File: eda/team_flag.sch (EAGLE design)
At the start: 19 parts, among them Q1 IRFML8244, Q2 IRFML8244

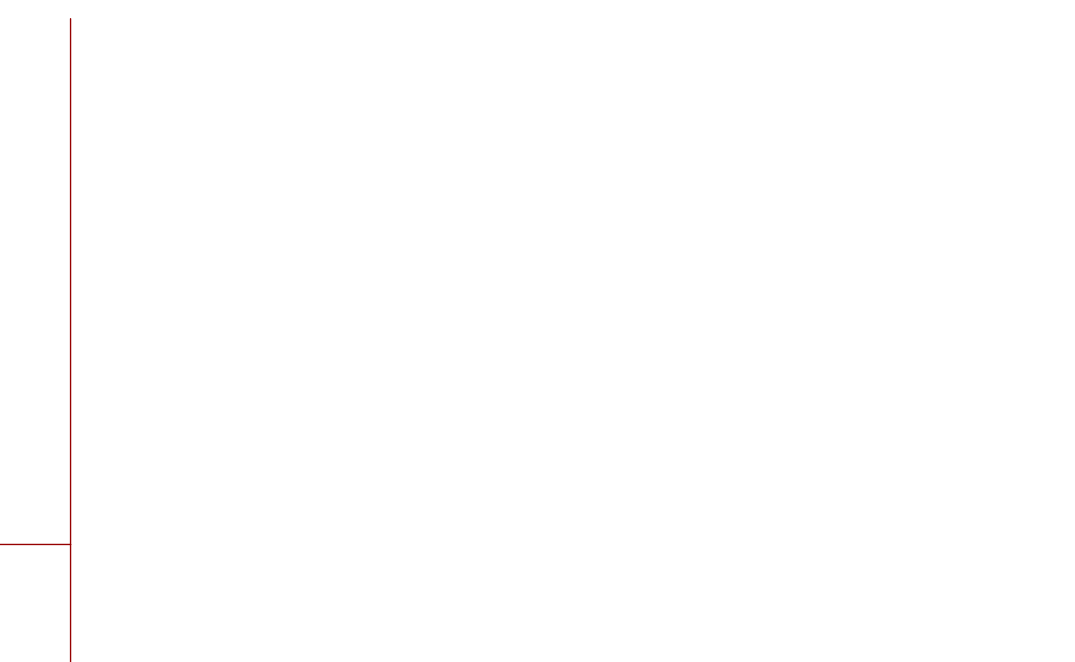
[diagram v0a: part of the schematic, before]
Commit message: Add Arduino Pro Micro breakout and connect nets on schematic
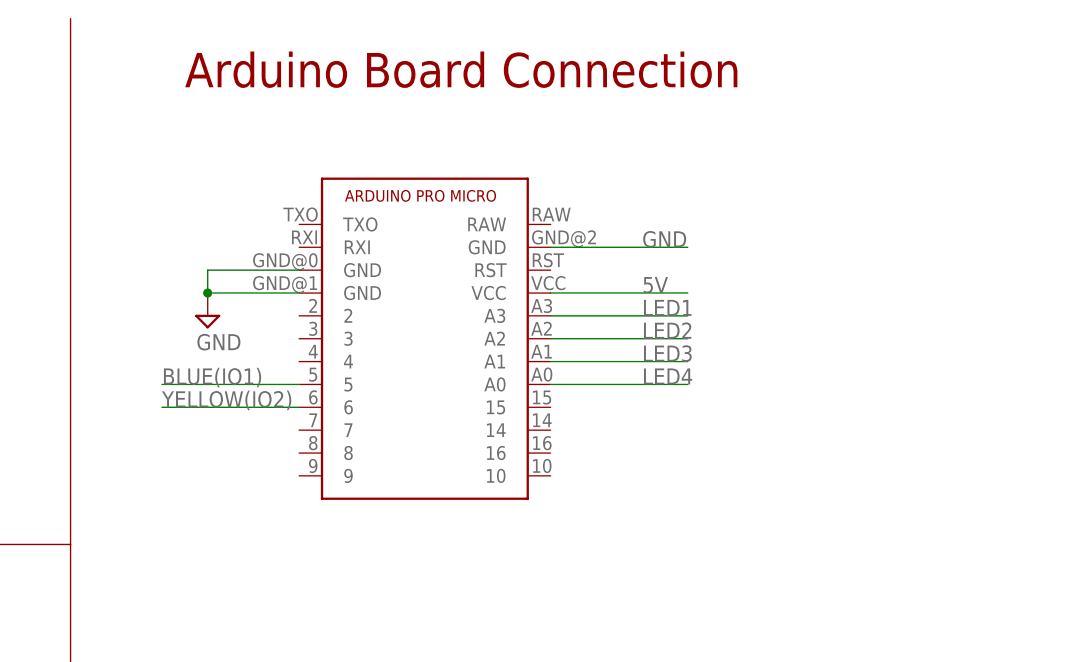
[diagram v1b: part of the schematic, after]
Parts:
- added U$3: ARDUINO_PRO_MICRO, pie:ARDUINO_PRO_MICRO
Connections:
- net 5V: now also U$3.VCC
- net BLUE(IO1): now also U$3.5
- net GND: now also U$3.GND@0, U$3.GND@1, U$3.GND@2
- net LED1: now also U$3.A3
- net LED2: now also U$3.A2
- net LED3: now also U$3.A1
- net LED4: now also U$3.A0
- net YELLOW(IO2): now also U$3.6
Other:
- note added: "Arduino Board Connection"
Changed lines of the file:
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@@
 <layer number="54" name="bGND_GNDA" color="1" fill="9" visible="no" active="no"/>
 <layer number="56" name="wert" color="7" fill="1" visible="no" active="no"/>
+<layer number="57" name="tCAD" color="7" fill="1" visible="no" active="no"/>
+<layer number="59" name="tCarbon" color="7" fill="1" visible="no" active="no"/>
+<layer number="60" name="bCarbon" color="7" fill="1" visible="no" active="no"/>
 <layer number="90" name="Modules" color="5" fill="1" visible="yes" active="yes"/>
 <layer number="91" name="Nets" color="2" fill="1" visible="yes" active="yes"/>
@@
 <layer number="109" name="fp9" color="7" fill="1" visible="yes" active="yes"/>
 <layer number="110" name="fp0" color="7" fill="1" visible="yes" active="yes"/>
+<layer number="111" name="LPC17xx" color="7" fill="1" visible="yes" active="yes"/>
+<layer number="112" name="tSilk" color="7" fill="1" visible="yes" active="yes"/>
+<layer number="113" name="IDFDebug" color="7" fill="1" visible="yes" active="yes"/>
+<layer number="114" name="Badge_Outline" color="11" fill="1" visible="no" active="no"/>
 <layer number="116" name="Patch_BOT" color="9" fill="4" visible="yes" active="yes"/>
+<layer number="118" name="Rect_Pads" color="7" fill="1" visible="yes" active="yes"/>
 <layer number="121" name="_tsilk" color="7" fill="1" visible="yes" active="yes"/>
 <layer number="122" name="_bsilk" color="7" fill="1" visible="yes" active="yes"/>
@@
 <layer number="124" name="bTestmark" color="7" fill="1" visible="yes" active="yes"/>
 <layer number="125" name="_tNames" color="7" fill="1" visible="yes" active="yes"/>
+<layer number="126" name="_bNames" color="7" fill="1" visible="yes" active="yes"/>
+<layer number="127" name="_tValues" color="7" fill="1" visible="yes" active="yes"/>
+<layer number="128" name="_bValues" color="7" fill="1" visible="yes" active="yes"/>
+<layer number="129" name="Mask" color="7" fill="1" visible="yes" active="yes"/>
 <layer number="131" name="tAdjust" color="7" fill="1" visible="yes" active="yes"/>
 <layer number="132" name="bAdjust" color="7" fill="1" visible="yes" active="yes"/>
 <layer number="144" name="Drill_legend" color="7" fill="1" visible="yes" active="yes"/>
+<layer number="150" name="Notes" color="7" fill="1" visible="yes" active="yes"/>
 <layer number="151" name="HeatSink" color="7" fill="1" visible="yes" active="yes"/>
+<layer number="152" name="_bDocu" color="7" fill="1" visible="yes" active="yes"/>
+<layer number="153" name="FabDoc1" color="7" fill="1" visible="yes" active="yes"/>
+<layer number="154" name="FabDoc2" color="7" fill="1" visible="yes" active="yes"/>
+<layer number="155" name="FabDoc3" color="7" fill="1" visible="yes" active="yes"/>
 <layer number="199" name="Contour" color="7" fill="1" visible="yes" active="yes"/>
 <layer number="200" name="200bmp" color="1" fill="10" visible="yes" active="yes"/>
@@
 <layer number="223" name="223bmp" color="24" fill="1" visible="no" active="no"/>
 <layer number="224" name="224bmp" color="25" fill="1" visible="no" active="no"/>
+<layer number="225" name="225bmp" color="7" fill="1" visible="yes" active="yes"/>
+<layer number="226" name="226bmp" color="7" fill="1" visible="yes" active="yes"/>
+<layer number="227" name="227bmp" color="7" fill="1" visible="yes" active="yes"/>
+<layer number="228" name="228bmp" color="7" fill="1" visible="yes" active="yes"/>
+<layer number="229" name="229bmp" color="7" fill="1" visible="yes" active="yes"/>
+<layer number="230" name="230bmp" color="7" fill="1" visible="yes" active="yes"/>
+<layer number="231" name="231bmp" color="7" fill="1" visible="yes" active="yes"/>
+<layer number="248" name="Housing" color="7" fill="1" visible="yes" active="yes"/>
+<layer number="249" name="Edge" color="7" fill="1" visible="yes" active="yes"/>
 <layer number="250" name="Descript" color="3" fill="1" visible="no" active="no"/>
 <layer number="251" name="SMDround" color="12" fill="11" visible="no" active="no"/>
 <layer number="254" name="cooling" color="7" fill="1" visible="yes" active="yes"/>
+<layer number="255" name="routoute" color="7" fill="1" visible="yes" active="yes"/>
 </layers>
 <schematic xreflabel="%F%N/%S.%C%R" xrefpart="/%S.%C%R">
@@
 <part name="LED4" library="pie" deviceset="LED" device="0805" value="RED"/>
 <part name="SUPPLY5" library="pie" deviceset="GND" device=""/>
+<part name="U$3" library="pie" deviceset="ARDUINO_PRO_MICRO" device=""/>
+<part name="SUPPLY6" library="pie" deviceset="GND" device=""/>
 </parts>
 <sheets>
@@
 <wire x1="109.22" y1="86.36" x2="109.22" y2="27.94" width="0.1524" layer="94"/>
 <wire x1="109.22" y1="27.94" x2="0" y2="27.94" width="0.1524" layer="94"/>
+<text x="121.92" y="177.8" size="3.81" layer="94" font="vector">Arduino Board Connection</text>
 </plain>
 <instances>
@@
 </instance>
 <instance part="SUPPLY5" gate="GND" x="78.74" y="35.56"/>
+<instance part="U$3" gate="G$1" x="147.32" y="149.86"/>
+<instance part="SUPPLY6" gate="GND" x="124.46" y="152.4"/>
 </instances>
 <busses>
@@
 <pinref part="JP2" gate="A" pin="4"/>
 <wire x1="27.94" y1="101.6" x2="48.26" y2="101.6" width="0.1524" layer="91"/>
+</segment>
+<segment>
+<pinref part="U$3" gate="G$1" pin="6"/>
+<label x="119.38" y="142.24" size="1.778" layer="95"/>
+<wire x1="134.62" y1="142.24" x2="119.38" y2="142.24" width="0.1524" layer="91"/>
 </segment>
 </net>
@@
 <wire x1="78.74" y1="40.64" x2="78.74" y2="38.1" width="0.1524" layer="91"/>
 </segment>
+<segment>
+<pinref part="U$3" gate="G$1" pin="GND@0"/>
+<wire x1="134.62" y1="157.48" x2="124.46" y2="157.48" width="0.1524" layer="91"/>
+<wire x1="124.46" y1="157.48" x2="124.46" y2="154.94" width="0.1524" layer="91"/>
+<pinref part="U$3" gate="G$1" pin="GND@1"/>
+<wire x1="124.46" y1="154.94" x2="134.62" y2="154.94" width="0.1524" layer="91"/>
+<pinref part="SUPPLY6" gate="GND" pin="GND"/>
+<junction x="124.46" y="154.94"/>
+</segment>
+<segment>
+<pinref part="U$3" gate="G$1" pin="GND@2"/>
+<wire x1="162.56" y1="160.02" x2="177.8" y2="160.02" width="0.1524" layer="91"/>
+<label x="172.72" y="160.02" size="1.778" layer="95"/>
+</segment>
 </net>
 <net name="BLUE(IO1)" class="0">
@@
 <wire x1="27.94" y1="104.14" x2="48.26" y2="104.14" width="0.1524" layer="91"/>
 </segment>
+<segment>
+<pinref part="U$3" gate="G$1" pin="5"/>
+<label x="119.38" y="144.78" size="1.778" layer="95"/>
+<wire x1="134.62" y1="144.78" x2="119.38" y2="144.78" width="0.1524" layer="91"/>
+</segment>
 </net>
 <net name="BSOURCE" class="0">
@@
 <label x="68.58" y="109.22" size="1.778" layer="95"/>
 </segment>
+<segment>
+<pinref part="U$3" gate="G$1" pin="VCC"/>
+<wire x1="162.56" y1="154.94" x2="177.8" y2="154.94" width="0.1524" layer="91"/>
+<label x="172.72" y="154.94" size="1.778" layer="95"/>
+</segment>
 </net>
 <net name="LED4" class="0">
@@
 <label x="68.58" y="99.06" size="1.778" layer="95"/>
 </segment>
+<segment>
+<pinref part="U$3" gate="G$1" pin="A0"/>
+<wire x1="162.56" y1="144.78" x2="177.8" y2="144.78" width="0.1524" layer="91"/>
+<label x="172.72" y="144.78" size="1.778" layer="95"/>
+</segment>
 </net>
 <net name="N$4" class="0">
@@
 <label x="68.58" y="106.68" size="1.778" layer="95"/>
 </segment>
+<segment>
+<pinref part="U$3" gate="G$1" pin="A3"/>
+<wire x1="162.56" y1="152.4" x2="177.8" y2="152.4" width="0.1524" layer="91"/>
+<label x="172.72" y="152.4" size="1.778" layer="95"/>
+</segment>
 </net>
 <net name="LED2" class="0">
@@
 <label x="68.58" y="104.14" size="1.778" layer="95"/>
 </segment>
+<segment>
+<pinref part="U$3" gate="G$1" pin="A2"/>
+<wire x1="162.56" y1="149.86" x2="177.8" y2="149.86" width="0.1524" layer="91"/>
+<label x="172.72" y="149.86" size="1.778" layer="95"/>
+</segment>
 </net>
 <net name="LED3" class="0">
@@
 <label x="68.58" y="101.6" size="1.778" layer="95"/>
 </segment>
-</net>
+<segment>
+<pinref part="U$3" gate="G$1" pin="A1"/>
+<wire x1="162.56" y1="147.32" x2="177.8" y2="147.32" width="0.1524" layer="91"/>
+<label x="172.72" y="147.32" size="1.778" layer="95"/>
+</segment>
+</net>

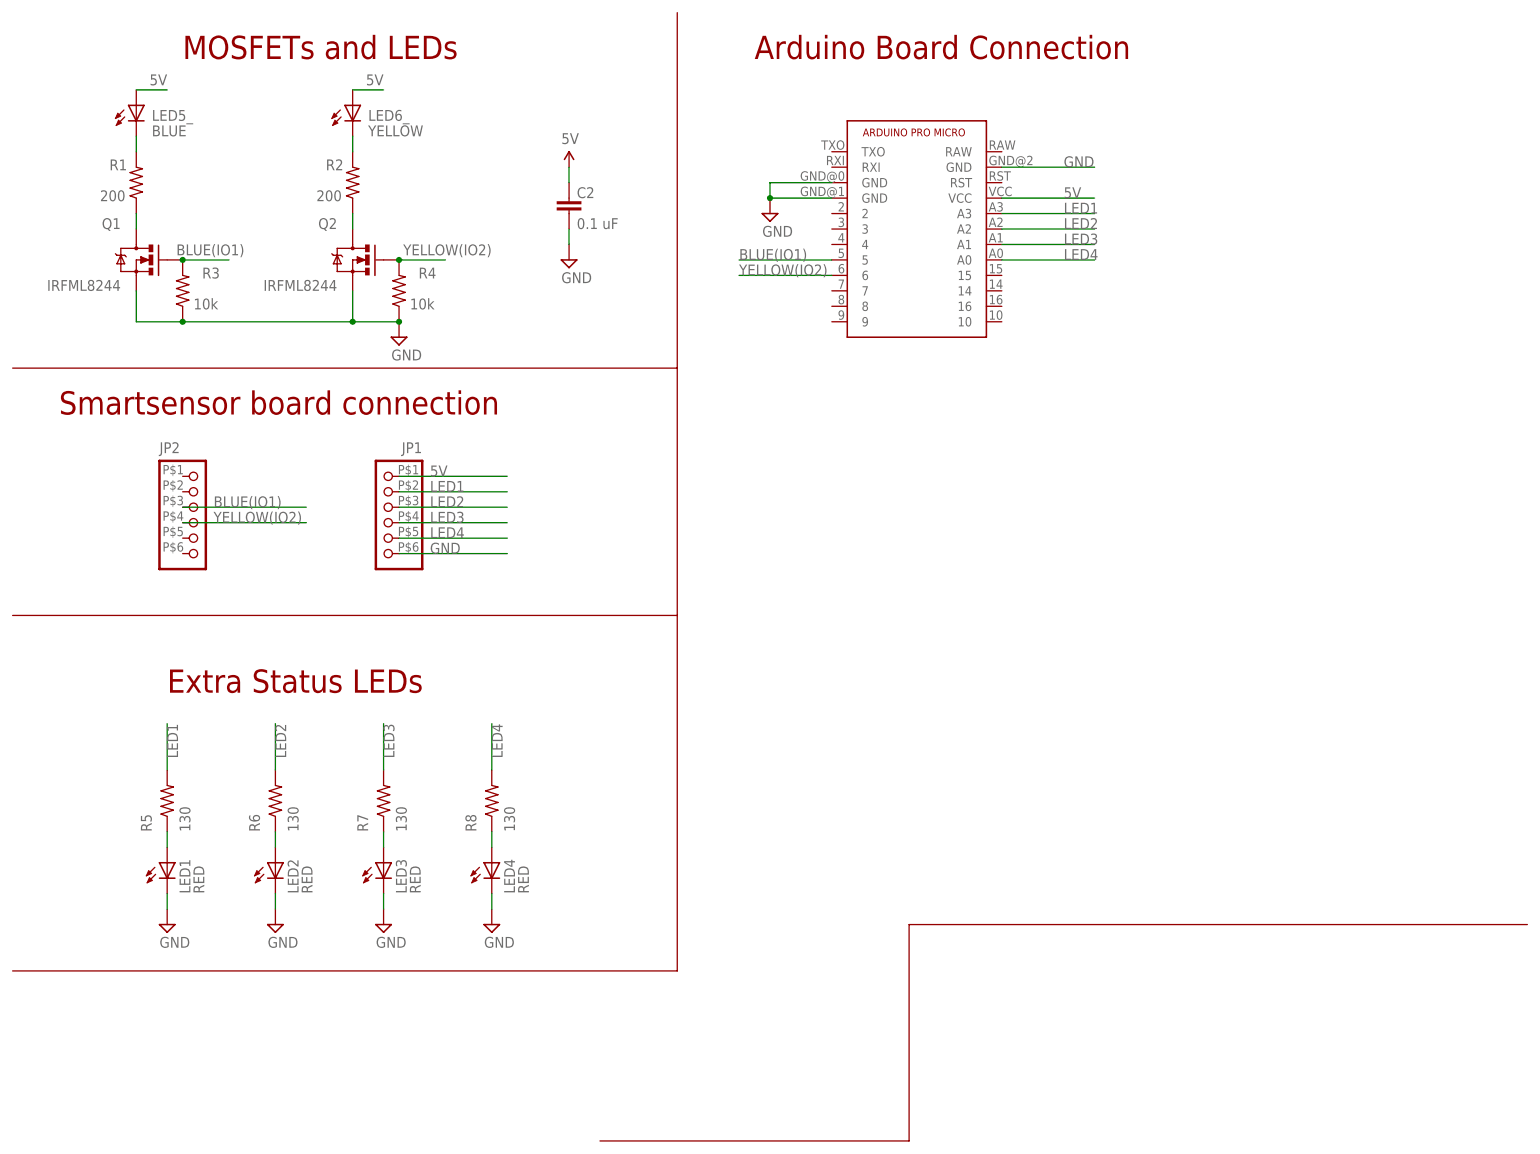
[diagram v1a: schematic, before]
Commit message: Finished routing team flag board (now with Arduino ProMicro)
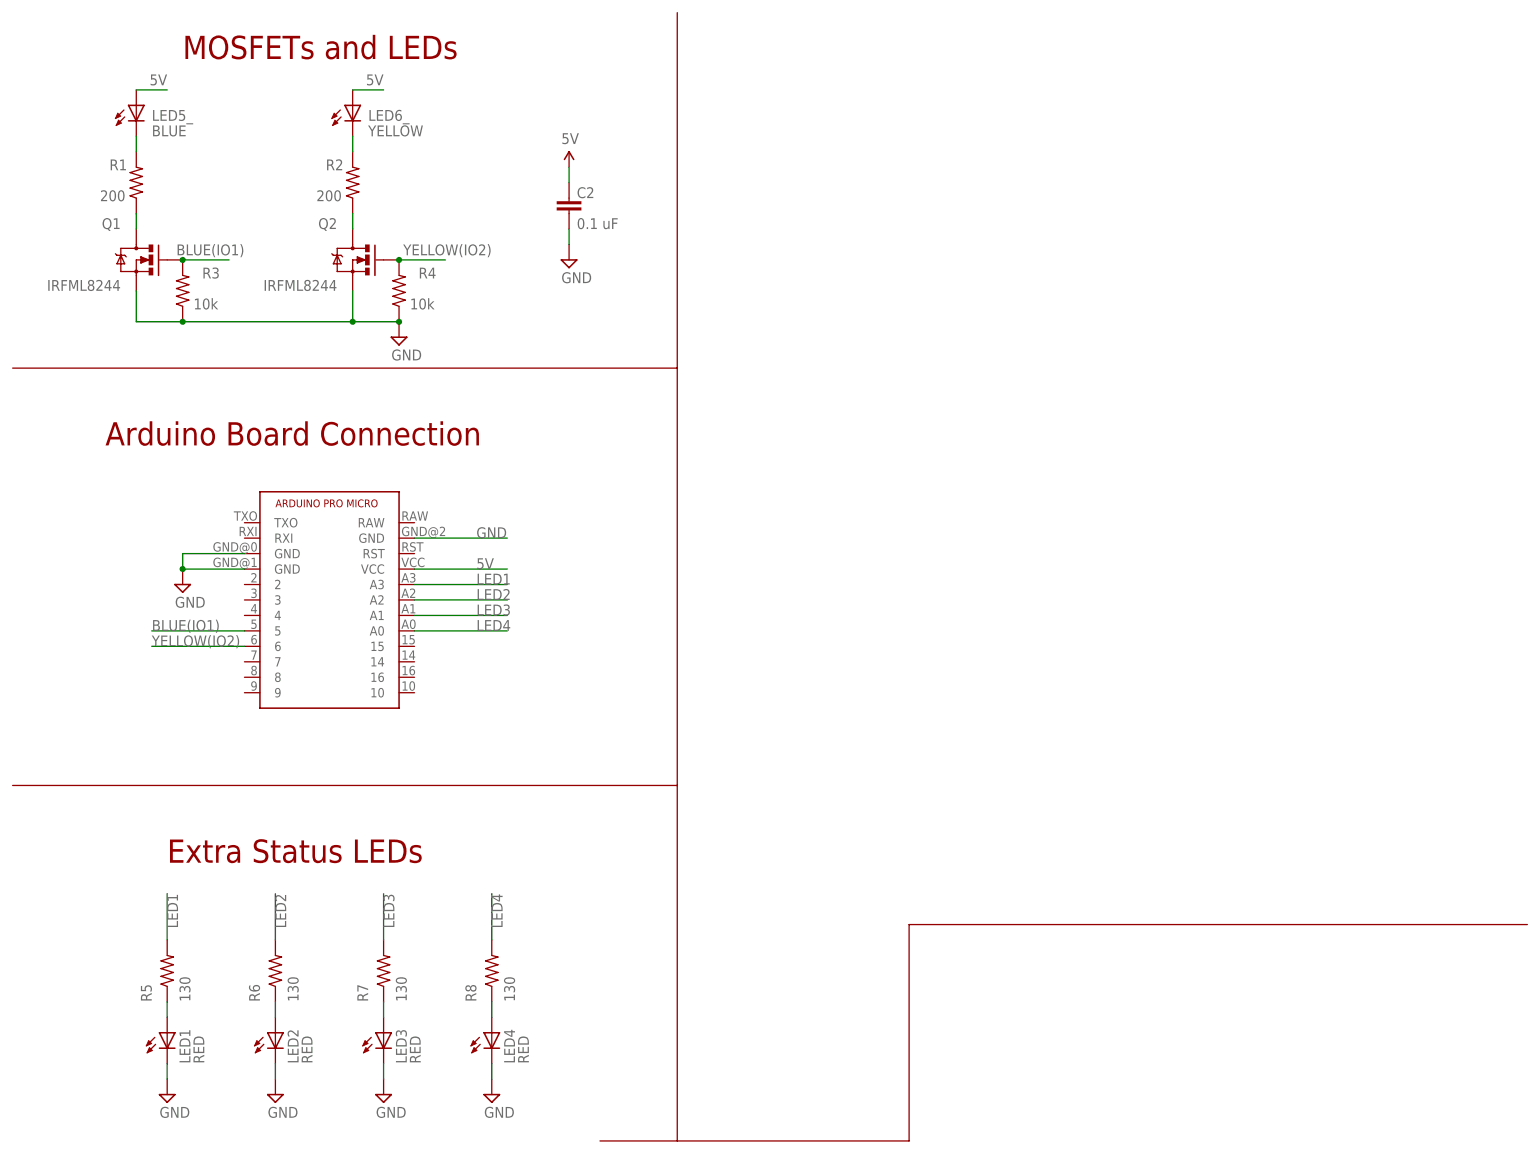
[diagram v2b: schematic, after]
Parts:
- removed JP1, JP2: (no value), pie:PINHD-1X6SMD-C
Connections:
- net N$1 renamed LED2R
- net N$4 renamed LED1R
- net N$5 renamed LED3R
- net N$6 renamed LED4R
- net 5V: no longer JP1.1
- net BLUE(IO1): no longer JP2.3
- net GND: no longer JP1.6
- net LED1: no longer JP1.2
- net LED2: no longer JP1.3
- net LED3: no longer JP1.4
- net LED4: no longer JP1.5
- net YELLOW(IO2): no longer JP2.4
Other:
- note removed: "Smartsensor board connection"
- moved on the sheet: LED1, LED2, LED3, LED4, R5, R6, R7, R8
